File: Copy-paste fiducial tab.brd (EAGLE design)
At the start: 3.8 x 88.9 mm, 1 part

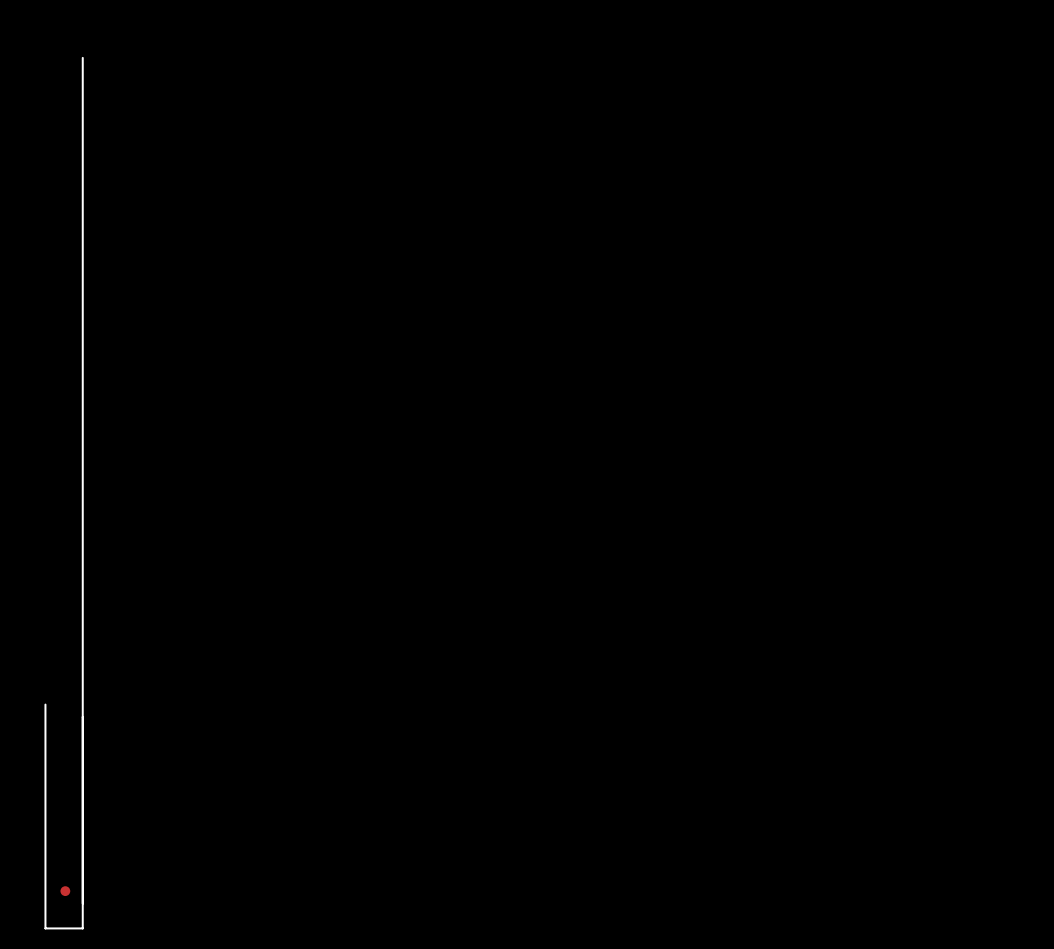
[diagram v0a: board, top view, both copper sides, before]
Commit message: Expanded rail to "5 wide"
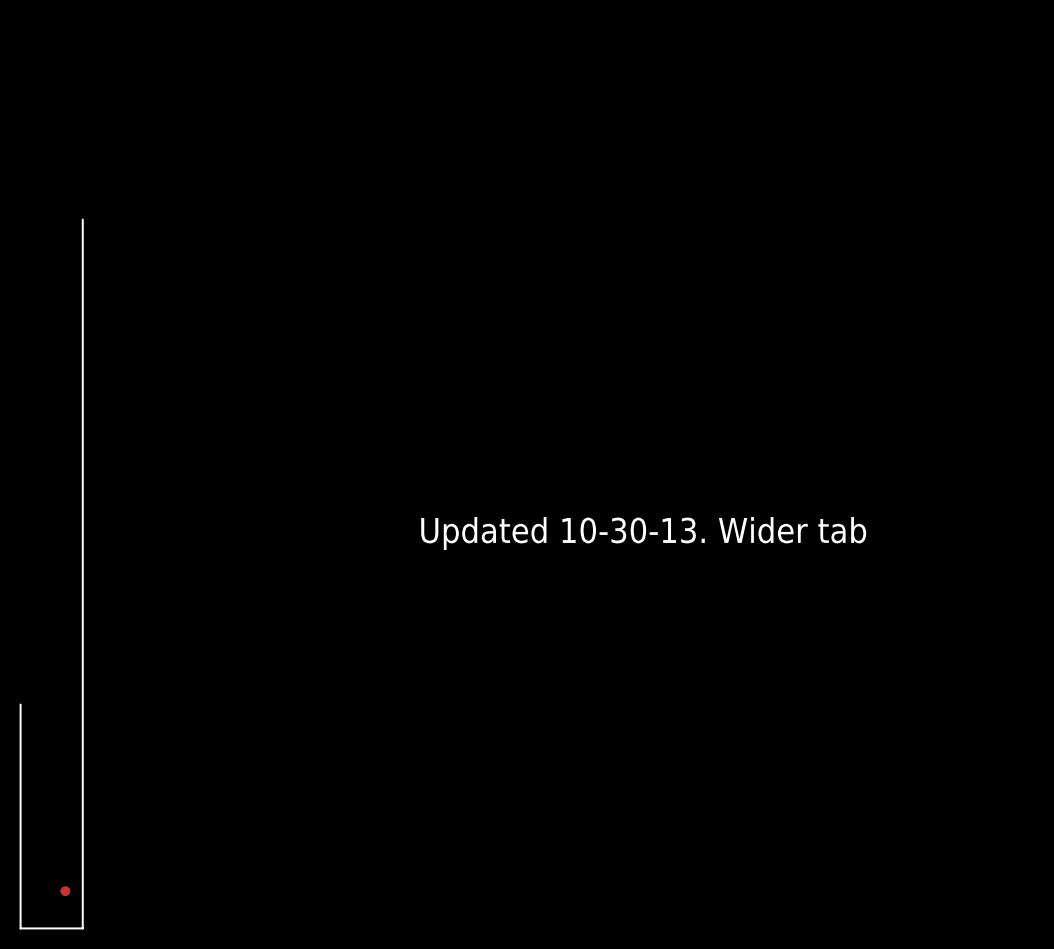
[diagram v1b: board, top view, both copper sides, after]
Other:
- board size 3.8 x 88.9 mm -> 6.3 x 72.4 mm
- board text added: "Updated 10-30-13. Wider tab"

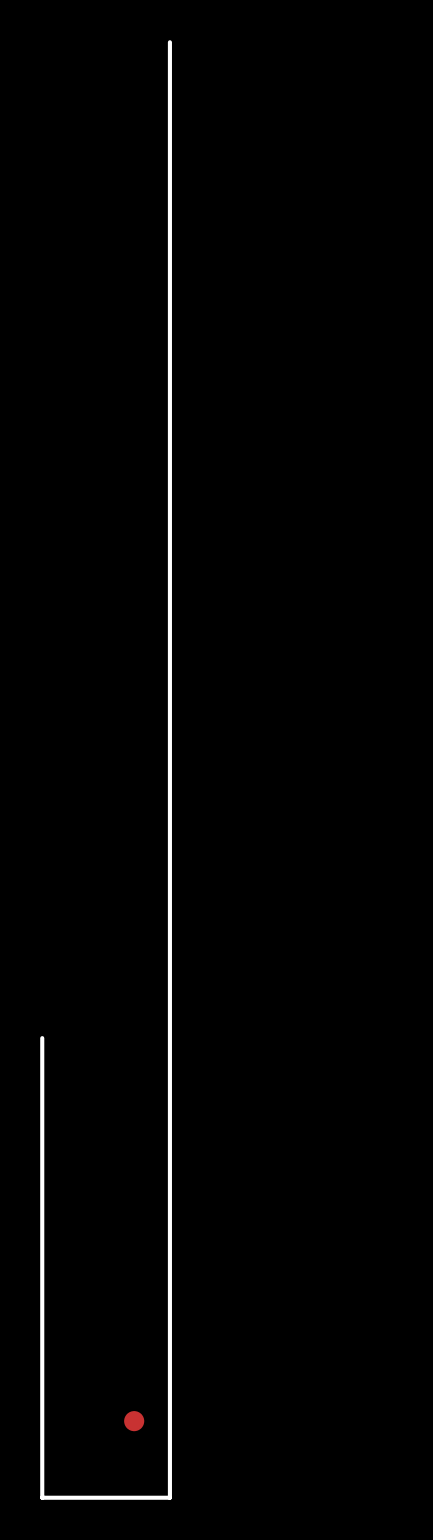
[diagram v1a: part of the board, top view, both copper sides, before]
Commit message: centered fiducial
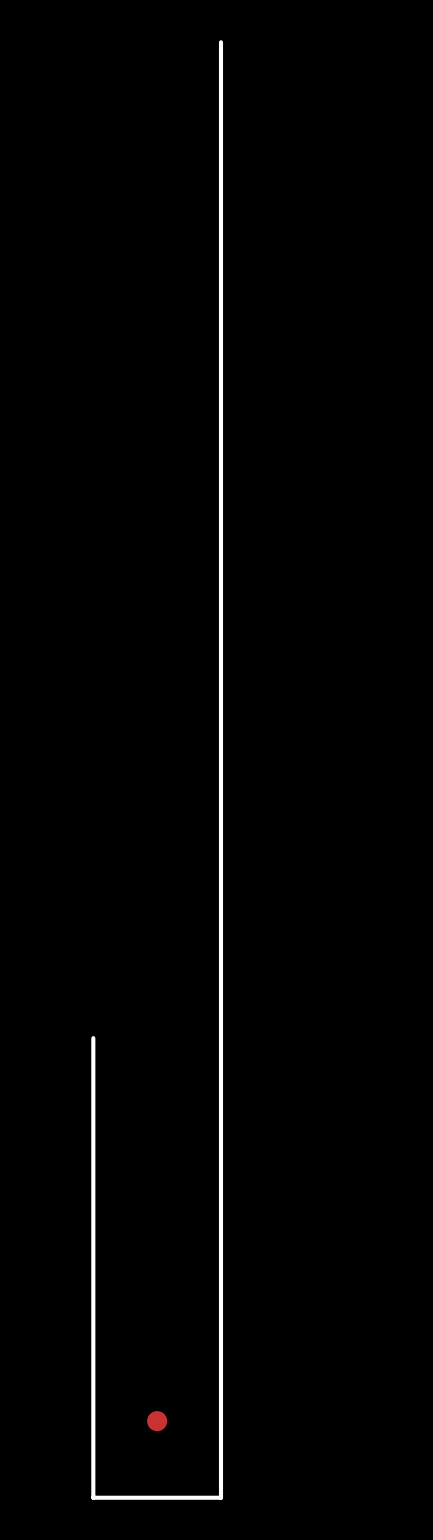
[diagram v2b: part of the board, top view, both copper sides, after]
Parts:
- moved E$1 1.14 mm to (3.17, 3.81)
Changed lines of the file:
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@@
 <board>
 <plain>
-<wire x1="3.81" y1="0" x2="3.81" y2="72.39" width="0.2032" layer="20"/>
-<wire x1="-2.54" y1="0" x2="3.81" y2="0" width="0.2032" layer="20"/>
-<wire x1="-2.54" y1="0" x2="-2.54" y2="22.86" width="0.2032" layer="20"/>
+<wire x1="6.35" y1="0" x2="6.35" y2="72.39" width="0.2032" layer="20"/>
+<wire x1="0" y1="0" x2="6.35" y2="0" width="0.2032" layer="20"/>
+<wire x1="0" y1="0" x2="0" y2="22.86" width="0.2032" layer="20"/>
 <text x="39.37" y="48.26" size="2.1844" layer="27" font="vector" ratio="12">Copy and paste into panel for fiducial tabs</text>
 <text x="38.1" y="39.37" size="2.54" layer="20" font="vector" ratio="7">Updated 10-30-13. Wider tab</text>
@@
 </autorouter>
 <elements>
-<element name="E$1" library="SparkFun-Aesthetics" package="FIDUCIAL-1X2" value="" x="2.032" y="3.81"/>
+<element name="E$1" library="SparkFun-Aesthetics" package="FIDUCIAL-1X2" value="" x="3.175" y="3.81"/>
 </elements>
 <signals>

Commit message: filled out full tab
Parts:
- added E$2: (no value), SparkFun-Aesthetics:FIDUCIAL-1X2
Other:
- board size 6.3 x 72.4 mm -> 6.3 x 92.7 mm
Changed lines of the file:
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@@
 <?xml version="1.0" encoding="utf-8"?>
 <!DOCTYPE eagle SYSTEM "eagle.dtd">
-<eagle version="6.5.0">
+<eagle version="7.3.0">
 <drawing>
 <settings>
@@
 <text x="39.37" y="48.26" size="2.1844" layer="27" font="vector" ratio="12">Copy and paste into panel for fiducial tabs</text>
 <text x="38.1" y="39.37" size="2.54" layer="20" font="vector" ratio="7">Updated 10-30-13. Wider tab</text>
+<wire x1="0" y1="92.71" x2="0" y2="20.32" width="0.2032" layer="20"/>
+<wire x1="6.35" y1="92.71" x2="0" y2="92.71" width="0.2032" layer="20"/>
+<wire x1="6.35" y1="92.71" x2="6.35" y2="69.85" width="0.2032" layer="20"/>
 </plain>
 <attributes>
@@
 <pass name="Default">
 <param name="RoutingGrid" value="50mil"/>
+<param name="AutoGrid" value="1"/>
+<param name="Efforts" value="0"/>
+<param name="TopRouterVariant" value="1"/>
 <param name="tpViaShape" value="round"/>
 <param name="PrefDir.1" value="|"/>
@@
 <elements>
 <element name="E$1" library="SparkFun-Aesthetics" package="FIDUCIAL-1X2" value="" x="3.175" y="3.81"/>
+<element name="E$2" library="SparkFun-Aesthetics" package="FIDUCIAL-1X2" value="" x="3.175" y="88.9" rot="R180"/>
 </elements>
 <signals>
